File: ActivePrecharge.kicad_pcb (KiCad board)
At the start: 2 copper layers, 82.5 x 63 mm, 59 parts, among them Con1 LED, J1 Conn_01x03, J2 Conn_01x02, J3 Conn_01x02, Q1 PMV35EPER, Q2 IRLML0030, U1 NCP785AH50T1G, U1I_TP1 TestPoint, U2 NCP785AH50T1G, U2I_TP1 TestPoint, U2O_TP1 TestPoint, U3 TLV9301xDCK, U4 TCMT1106

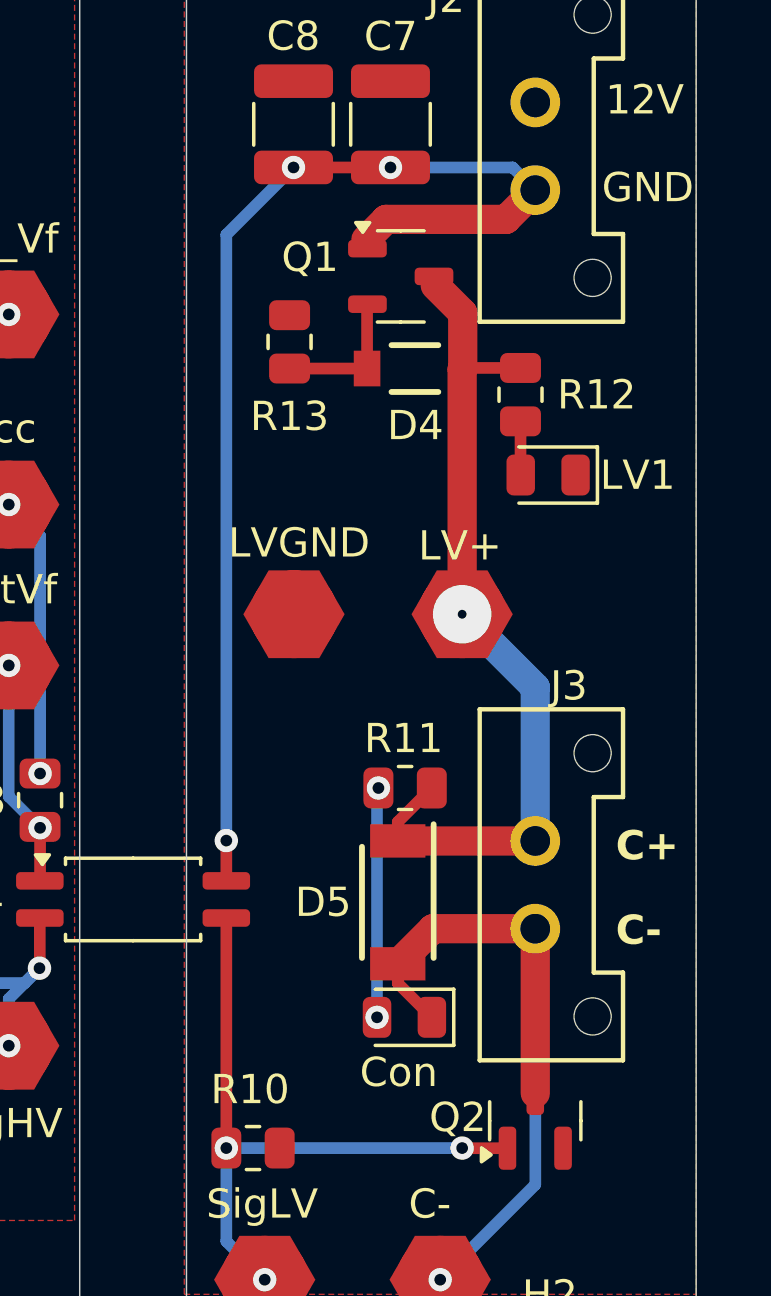
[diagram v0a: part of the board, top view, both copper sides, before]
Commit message: fixed pmos orientation on LV reverse polarity protection, was s and d were backwards
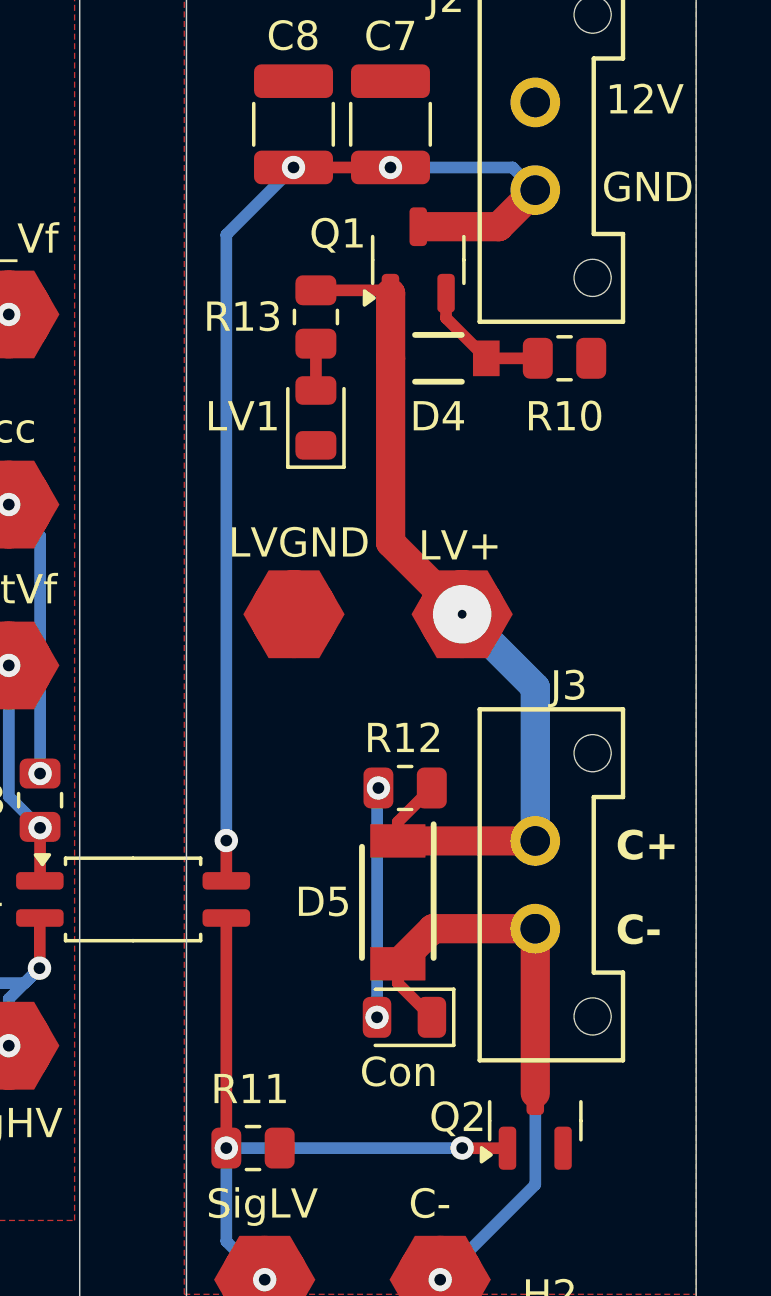
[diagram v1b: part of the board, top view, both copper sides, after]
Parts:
- R1: value 110k -> 120k
- moved R10 9.42 mm to (142.0, 86.0), turned to 180 degrees
- moved LV1 8.18 mm to (133.5, 88.0), turned to 90 degrees
- moved R13 7.48 mm to (133.5, 84.6)
- moved D4 0.88 mm to (137.7, 86.0), turned to 0 degrees
- moved Q1 0.82 mm to (137.0, 82.6), turned to 90 degrees
- renumbered R13 to R10, R10 to R11, R11 to R12, R12 to R13
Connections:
- Q1 pad 1: +12V -> /LV+
- Q1 pad 3: /LV+ -> +12V
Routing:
- net +12V: track 40.4 -> 38.2 mm
- net /LV+: track 29.4 -> 30.4 mm

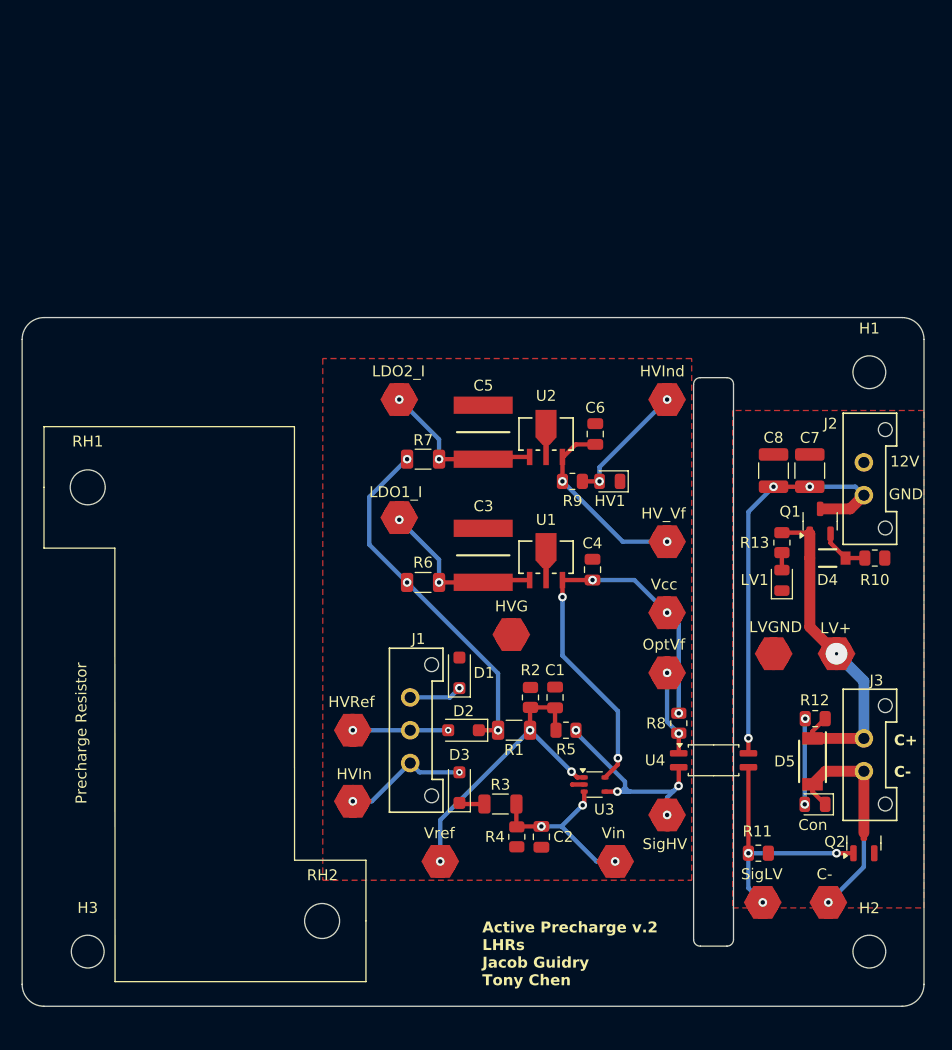
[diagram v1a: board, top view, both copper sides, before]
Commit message: HV Layout w/ components on the back
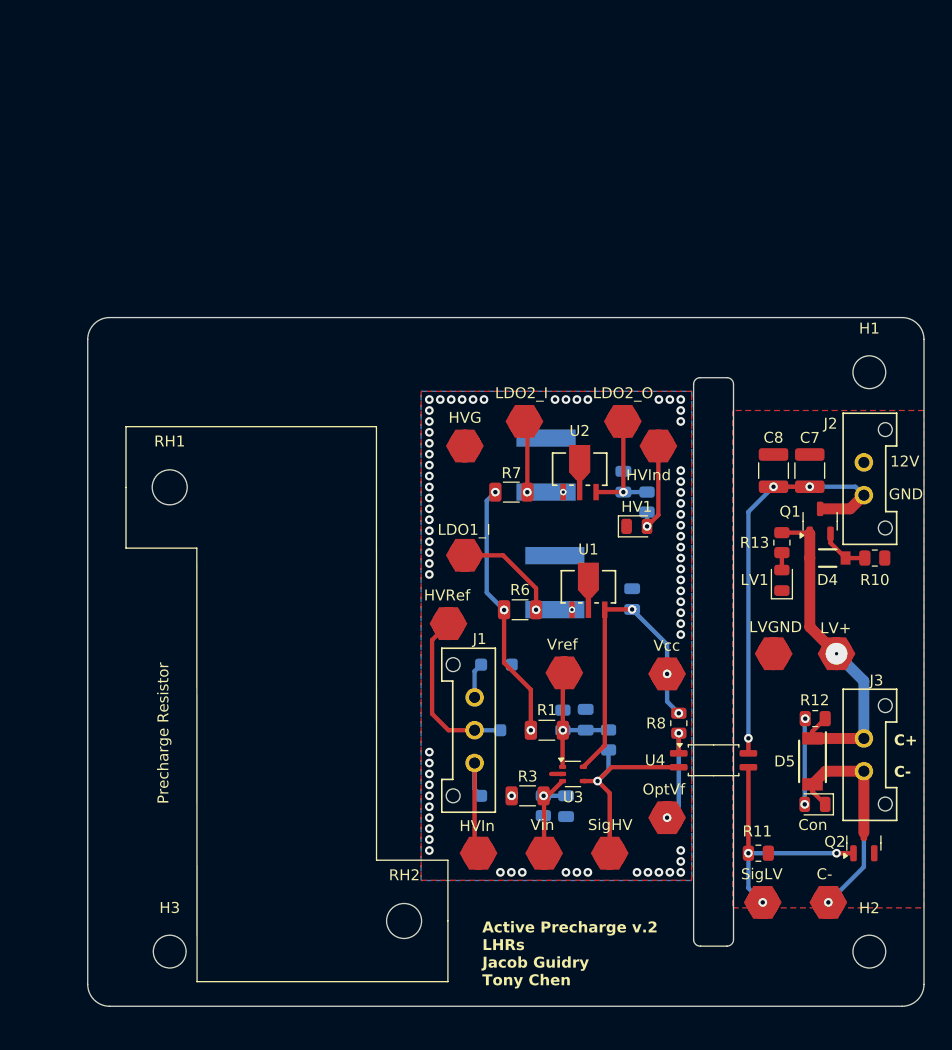
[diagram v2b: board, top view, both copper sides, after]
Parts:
- C1, C2, C3, C4, C5, C6, D1, D2, D3, R2, R4, R5, R9: moved to B.Cu
- moved Ref_TP1 20.6 mm to (113.6, 96.5)
- moved HVG_TP1 17.8 mm to (104.5, 75.8)
- moved OptVf_TP1 13.2 mm to (123.0, 109.8)
- moved HVR_TP1 13.1 mm to (103.0, 92.0)
- moved HVI_TP1 12.4 mm to (105.8, 113.0)
- moved U2O_TP1 11.7 mm to (119.0, 73.5)
- moved U2I_TP1 11.6 mm to (110.0, 73.5)
- moved R6 9.22 mm to (109.5, 90.7)
- moved R7 8.62 mm to (108.8, 80.0)
- moved J1 8.41 mm to (105.4, 104.8), turned to 90 degrees
- moved H3 7.50 mm to (77.5, 122.0)
- moved RH1 7.50 mm to (77.5, 79.5)
- moved RH2 7.50 mm to (98.9, 119.2)
- moved R9 7.08 mm to (121.2, 80.9), turned to -90 degrees
- moved C3 7.01 mm to (112.7, 88.2)
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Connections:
- J1 pad 1: HVGND -> /HVIn
- J1 pad 3: /HVIn -> HVGND
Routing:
- net /Vref: track 28.6 -> 12.9 mm, vias 3 -> 1
- net /Vcc+: track 41.1 -> 29.0 mm, vias 5 -> 3
- net /HRef: track 32.9 -> 23.8 mm
- net Net-(U2-VIN): track 15.3 -> 6.58 mm
- net HVRef: track 8.73 -> 15.7 mm, vias 2 -> 0
- net /Vin: track 16.5 -> 9.62 mm, vias 3 -> 1
- net Net-(U2-VOUT): track 17.6 -> 11.1 mm, vias 2 -> 1
- net Net-(U1-VIN): track 15.6 -> 9.73 mm
- net Net-(HV1-A): track 11.6 -> 9.09 mm, vias 2 -> 1
- net /HIn: track 2.33 -> 0.00 mm, vias 0 -> 1
- net Net-(OptVf_TP1-Pad1): track 7.84 -> 10.0 mm
- net /SignalHV: track 21.4 -> 19.6 mm, vias 4 -> 1
- net HVGND: track 4.85 -> 3.25 mm, vias 1 -> 0
- net /HVIn: track 11.6 -> 11.8 mm, vias 2 -> 0
- net /HGND: track 1.13 -> 1.05 mm, vias 0 -> 70
- added copper zone on B.Cu, net /HGND
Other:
- board size 82.5 x 63 mm -> 76.5 x 63 mm
- board text added: "LDO2_O"
- board text removed: "HV_Vf"

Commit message: components places on both sides of the board for HV and LV sides, ready for review
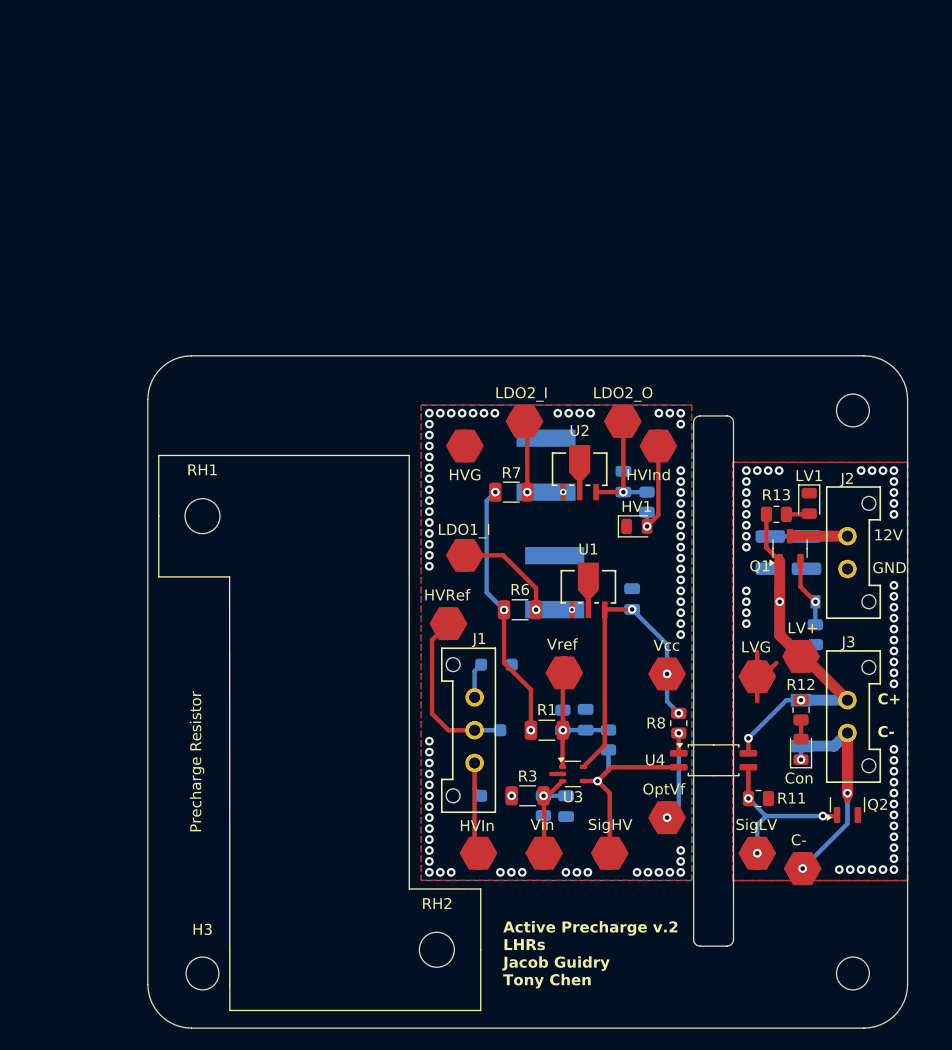
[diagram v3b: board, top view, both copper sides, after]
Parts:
- C7, C8, D4, D5, R10: moved to B.Cu
- moved R10 8.87 mm to (136.6, 93.0), turned to 90 degrees
- moved C7 8.33 mm to (132.4, 85.5), turned to -90 degrees
- moved C8 8.08 mm to (135.8, 85.5), turned to -90 degrees
- moved LV1 7.47 mm to (136.0, 81.0), turned to -90 degrees
- moved J2 6.91 mm to (139.5, 84.0)
- moved Con1 5.19 mm to (135.2, 103.5), turned to 90 degrees
- moved R11 5.00 mm to (131.4, 108.0)
- moved D4 4.85 mm to (134.9, 90.0)
- moved SigLV_TP1 4.53 mm to (131.2, 113.0)
- moved RH1 3.99 mm to (80.5, 82.2)
- moved RH2 3.99 mm to (101.9, 121.8)
- moved Con-_TP1 3.89 mm to (135.4, 114.4)
- moved H1 3.81 mm to (140.0, 72.5)
- moved J3 3.81 mm to (139.5, 99.0)
- moved Q2 3.81 mm to (139.5, 108.6)
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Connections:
- 12V_TP1 pad 1: /LV+ -> LV+
- D4 pad 1: /LV+ -> LV+
- D5 pad 1: /LV+ -> LV+
- J2 pad 1: LVGND -> +12V
- J2 pad 2: +12V -> LVGND
- J3 pad 1: /LV+ -> LV+
- Q1 pad 1: /LV+ -> LV+
- R12 pad 2: /LV+ -> LV+
- R13 pad 1: /LV+ -> LV+
- U4 pad 4: +12V -> LV+
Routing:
- net LV+: track 0.00 -> 32.1 mm, vias 0 -> 3
- net /LV+: track 30.4 -> 0.00 mm, vias 1 -> 0
- net +12V: track 38.2 -> 12.0 mm, vias 3 -> 0
- net /SignalLV: track 22.5 -> 15.4 mm
- net Net-(Con1-K): track 26.5 -> 20.2 mm, vias 1 -> 3
- net LVGND: track 0.00 -> 6.27 mm, vias 0 -> 50
- net Net-(Con1-A): track 7.86 -> 1.75 mm, vias 2 -> 0
- net Net-(D4-A): track 4.56 -> 6.40 mm, vias 0 -> 1
- net Net-(LV1-A): track 1.60 -> 2.11 mm
- net /HGND: vias 70 -> 73
- added copper zone on B.Cu, net LVGND
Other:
- board size 76.5 x 63 mm -> 69.5 x 61.5 mm
- board text added: "LVG"
- board text removed: "LVGND"

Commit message: sch done for workday 11/16/2024
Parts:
- added IC1: 1769205241, Active-PrechargeLib:1769205241, F.Cu at (110.2, 43.0)
- added LV2: LED, LED_SMD:LED_0805_2012Metric, F.Cu at (139.1, 56.5)
- added Q2: PMV35EPER, Package_TO_SOT_SMD:SOT-23-3, F.Cu at (129.4, 57.4)
- added Q3: IRLML0030, Package_TO_SOT_SMD:SOT-23, F.Cu at (134.4, 57.4)
- added R6: 50k, Resistor_SMD:R_0805_2012Metric, F.Cu at (139.7, 41.2)
- added R7: 500k, Resistor_SMD:R_1206_3216Metric, F.Cu at (124.0, 56.6)
- added R9: 640, Resistor_SMD:R_0805_2012Metric, F.Cu at (139.7, 44.1)
- C7, C8: value 47u -> 10u
- R1: value 120k -> 620k
- R12: value 5k -> 1k
- R13: value 5k -> 2k
- R2, R4: value 1k -> 5k
- R3: value 100k -> 500k
- R5: value 44.2k -> 200k
- R8: value 1.91k -> 380
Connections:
- net /Vref renamed Net-(U3-+)
- net HVRef renamed HRef
- 12V_TP1 pad 1: LV+ -> /LV+
- C1 pad 2: /HGND -> /HVGND
- C2 pad 2: /HGND -> /HVGND
- Con-_TP1 pad 1: Net-(Con1-K) -> Net-(D5-K)
- Con1 pad 1: Net-(Con1-K) -> GND
- D1 pad 1: HVGND -> HGND
- D1 pad 2: /HGND -> /HVGND
- D2 pad 1: /HRef -> /HVRef
- D3 pad 1: /HIn -> /HVIn
- D3 pad 2: /HVIn -> /HIn
- D4 pad 1: LV+ -> /LV+
- D5 pad 1: LV+ -> Net-(D5-K)
- D5 pad 2: Net-(Con1-K) -> GND
- HVG_TP1 pad 1: /HGND -> /HVGND
- HVI_TP1 pad 1: /HVIn -> /HIn
- J1 pad 1: /HVIn -> /HIn
- J1 pad 3: HVGND -> HGND
- J3 pad 1: LV+ -> Net-(D5-K)
- J3 pad 2: Net-(Con1-K) -> GND
- Q1 pad 1: LV+ -> /LV+
- R1 pad 1: /HRef -> /HVRef
- R12 pad 2: LV+ -> Net-(D5-K)
- R13 pad 1: LV+ -> /LV+
- R2 pad 2: /HGND -> /HVGND
- R3 pad 1: /HIn -> /Vin
- R3 pad 2: /Vin -> /HVIn
- R4 pad 2: /HGND -> /HVGND
- R5 pad 2: /SignalHV -> Net-(Q3-D)
- R8 pad 2: /Vcc+ -> /SignalHV
- SigHV_TP1 pad 1: /SignalHV -> Net-(Q3-D)
- U3 pad 2: /HGND -> HGND
- U3 pad 4: /SignalHV -> Net-(Q3-D)
- U4 pad 2: /SignalHV -> /HVGND
- U4 pad 4: LV+ -> +12V
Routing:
- net LV+: track 32.1 -> 0.00 mm, vias 3 -> 0
- net +12V: track 12.0 -> 44.1 mm, vias 0 -> 3
- net /HVIn: track 11.8 -> 0.00 mm
- net /HIn: track 0.00 -> 11.8 mm
- net LVGND: track 6.27 -> 0.00 mm, vias 50 -> 46
- net HGND: track 0.00 -> 4.30 mm, vias 0 -> 57
- net HVGND: track 3.25 -> 0.00 mm
- net /HGND: track 1.05 -> 0.00 mm, vias 73 -> 0
- added copper zone on B.Cu, net /HVGND
- added copper zone on F.Cu, net /HVGND
- removed copper zone on B.Cu, net /HGND
- removed copper zone on F.Cu, net /HGND
